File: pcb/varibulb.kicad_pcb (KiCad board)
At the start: 2 copper layers, 53.8 x 53.8 mm, 41 parts, among them IC1 ATTINY2313A-S, P1 MAINS LIVE, P2 BOARD, P3 BOARD, P5 MAINS GROUND, P6 ISP, P7 COMM, SW1 ENCODER, U1 TRIAC, U2 LM2931AZ-3.3/5.0, X1 10MHz

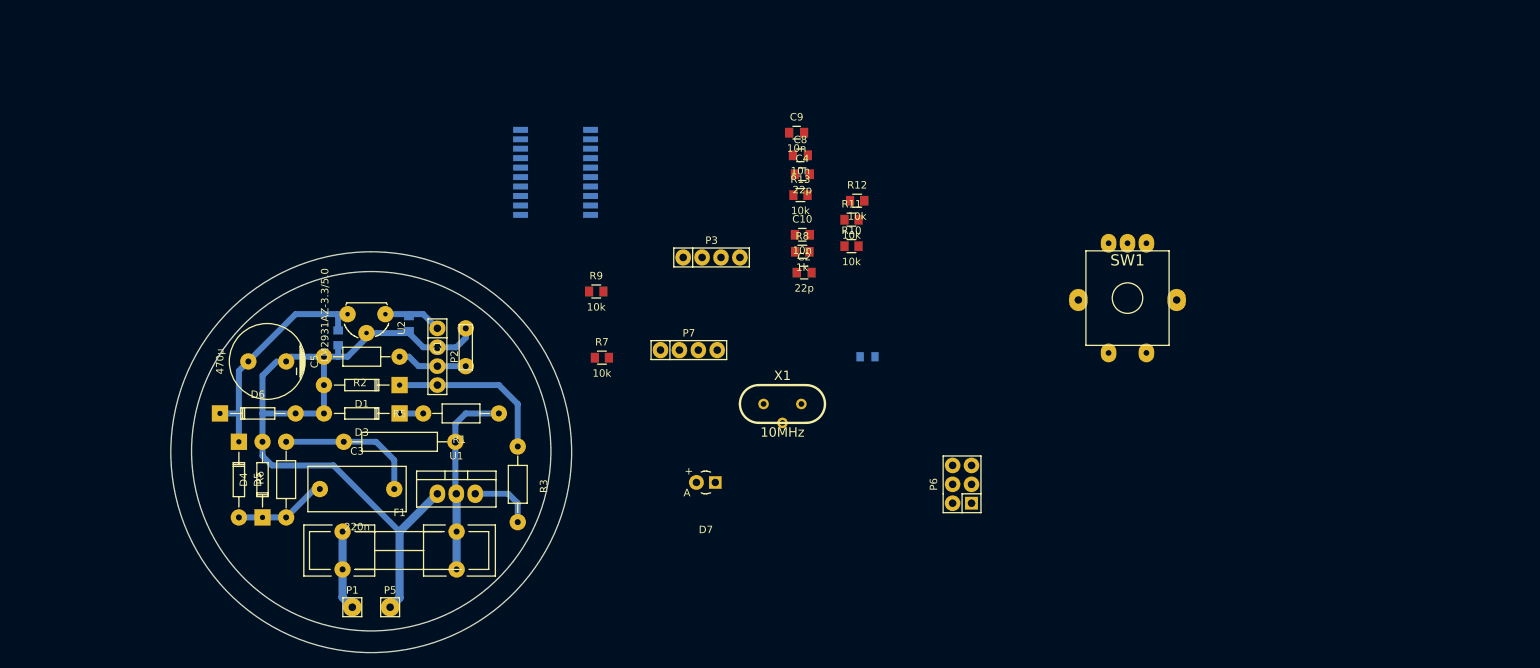
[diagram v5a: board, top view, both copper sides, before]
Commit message: move capacitor
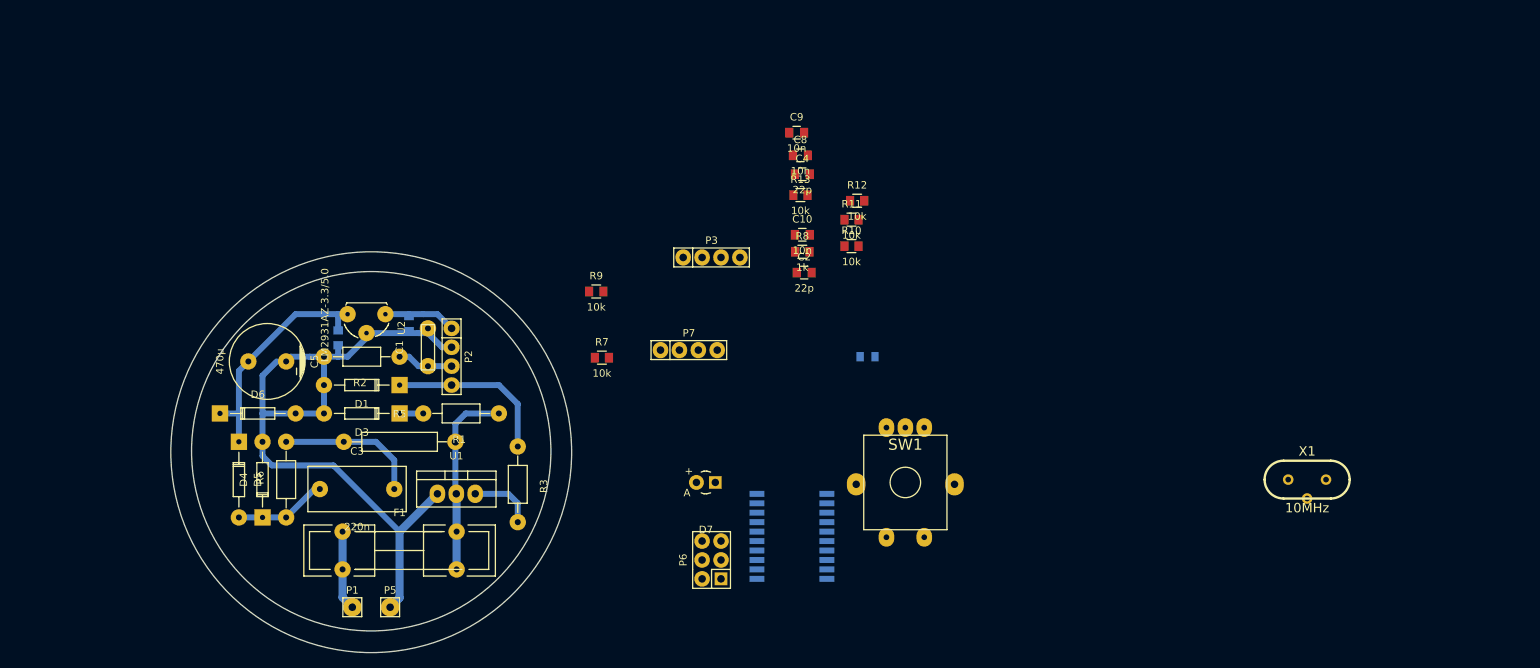
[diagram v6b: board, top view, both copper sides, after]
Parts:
- moved X1 71.2 mm to (196.8, 125.1)
- moved IC1 58.3 mm to (127.6, 132.7)
- moved SW1 38.8 mm to (142.9, 125.7)
- moved P6 35.2 mm to (116.8, 135.9)
- moved C1 5.08 mm to (78.7, 107.3)
- moved P2 1.91 mm to (81.9, 108.6)
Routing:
- net GNDREF: track 99.7 -> 97.5 mm
- net Net-(C7-Pad2): track 8.04 -> 9.95 mm
- net Net-(C1-Pad1): track 13.2 -> 11.3 mm
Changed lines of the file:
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@@
   (general
     (links 86)
-    (no_connects 52)
+    (no_connects 53)
     (area 44.755999 93.777999 98.754001 147.776001)
     (thickness 1.6)
     (drawings 2)
-    (tracks 72)
+    (tracks 73)
     (zones 0)
     (modules 41)
@@
   )
   (module Capacitors_ThroughHole:Capacitor6MMDiscRM5 (layer F.Cu)
-    (at 83.82 107.315 90)
+    (at 78.74 107.315 90)
     (descr "Capacitor 6MM Disc RM 5MM")
     (tags C)
@@
   )
   (module Pin_Headers:Pin_Header_Straight_2x03 (layer F.Cu)
-    (at 150.495 125.73 90)
+    (at 116.84 135.89 90)
     (descr "Through hole pin header")
     (tags "pin header")
@@
   )
   (module encoder:ENCODER (layer F.Cu)
-    (at 172.72 100.965 180)
+    (at 142.875 125.73 180)
     (fp_text reference SW1 (at 0 5.334 180) (layer F.SilkS)
       (effects (font (size 1.5 1.5) (thickness 0.15)))
@@
   )
   (module HC-49V:HC-49V (layer F.Cu)
-    (at 126.365 114.935)
+    (at 196.85 125.095)
     (descr "Quartz boitier HC-49 Vertical Shielded")
     (tags "QUARTZ DEV")
@@
   )
   (module Housings_SOIC:SOIC-20_7.5x12.8mm_Pitch1.27mm (layer B.Cu)
-    (at 95.885 83.82 180)
+    (at 127.635 132.715 180)
     (descr "20-Lead Plastic Small Outline (SO) - Wide, 7.50 mm Body [SOIC] (see Microchip Packaging Specification 00000049BS.pdf)")
     (tags "SOIC 1.27")
@@
   )
   (module Pin_Headers:Pin_Header_Straight_1x04 (layer F.Cu)
-    (at 80.01 108.585 270)
+    (at 81.915 108.585 270)
     (descr "Through hole pin header")
     (tags "pin header")
@@
   (segment (start 90.805 128.27) (end 89.535 127) (width 0.8) (layer B.Cu) (net 23))
   (segment (start 89.535 127) (end 85.09 127) (width 0.8) (layer B.Cu) (net 23))
-  (segment (start 80.01 109.855) (end 83.82 109.855) (width 0.8) (layer B.Cu) (net 24))
   (segment (start 74.93 108.585) (end 76.2 108.585) (width 0.8) (layer B.Cu) (net 24))
-  (segment (start 77.47 109.855) (end 80.01 109.855) (width 0.8) (layer B.Cu) (net 24))
+  (segment (start 77.47 109.855) (end 81.915 109.855) (width 0.8) (layer B.Cu) (net 24) (status 20))
   (segment (start 76.2 108.585) (end 77.47 109.855) (width 0.8) (layer B.Cu) (net 24))
   (segment (start 78.105 116.205) (end 74.93 116.205) (width 0.8) (layer B.Cu) (net 24))
   (segment (start 75.565 108.585) (end 74.93 108.585) (width 0.8) (layer B.Cu) (net 24))
-  (segment (start 56.515 120.015) (end 56.515 121.92) (width 0.8) (layer B.Cu) (net 25) (status 400000))
+  (segment (start 76.2 105.14) (end 76.2 105.41) (width 0.8) (layer B.Cu) (net 25) (status 10))
+  (segment (start 78.74 104.775) (end 78.105 105.41) (width 0.8) (layer B.Cu) (net 25))
+  (segment (start 78.105 105.41) (end 77.47 105.41) (width 0.8) (layer B.Cu) (net 25))
+  (segment (start 70.485 105.41) (end 76.2 105.41) (width 0.8) (layer B.Cu) (net 25))
+  (segment (start 76.2 105.41) (end 77.47 105.41) (width 0.8) (layer B.Cu) (net 25))
+  (segment (start 77.47 105.41) (end 78.74 105.41) (width 0.8) (layer B.Cu) (net 25))
+  (segment (start 80.645 107.315) (end 81.915 107.315) (width 0.8) (layer B.Cu) (net 25) (status 20))
+  (segment (start 78.74 105.41) (end 80.645 107.315) (width 0.8) (layer B.Cu) (net 25))
+  (segment (start 56.515 120.015) (end 56.515 121.92) (width 0.8) (layer B.Cu) (net 25))
   (segment (start 66.04 123.19) (end 57.785 123.19) (width 0.8) (layer B.Cu) (net 25))
   (segment (start 66.04 123.19) (end 74.93 132.08) (width 0.8) (layer B.Cu) (net 25))
   (segment (start 56.515 121.92) (end 57.785 123.19) (width 0.8) (layer B.Cu) (net 25))
-  (segment (start 80.01 127) (end 74.93 132.08) (width 1.1) (layer B.Cu) (net 25) (status 400000))
-  (segment (start 74.93 140.97) (end 73.66 142.24) (width 1.1) (layer B.Cu) (net 25) (status 800000))
+  (segment (start 80.01 127) (end 74.93 132.08) (width 1.1) (layer B.Cu) (net 25))
+  (segment (start 74.93 140.97) (end 73.66 142.24) (width 1.1) (layer B.Cu) (net 25))
   (segment (start 74.93 132.08) (end 74.93 140.97) (width 1.1) (layer B.Cu) (net 25))
   (segment (start 66.675 107.045) (end 66.675 108.585) (width 0.8) (layer B.Cu) (net 25))
-  (segment (start 76.2 105.14) (end 76.2 105.41) (width 0.8) (layer B.Cu) (net 25) (status 10))
-  (segment (start 70.485 105.41) (end 76.2 105.41) (width 0.8) (layer B.Cu) (net 25))
-  (segment (start 78.105 107.315) (end 80.01 107.315) (width 0.8) (layer B.Cu) (net 25))
-  (segment (start 76.2 105.41) (end 78.105 107.315) (width 0.8) (layer B.Cu) (net 25))
-  (segment (start 80.01 107.315) (end 82.55 107.315) (width 0.8) (layer B.Cu) (net 25))
-  (segment (start 83.82 106.045) (end 83.82 104.775) (width 0.8) (layer B.Cu) (net 25))
-  (segment (start 82.55 107.315) (end 83.82 106.045) (width 0.8) (layer B.Cu) (net 25))
   (segment (start 64.77 108.585) (end 66.675 108.585) (width 0.8) (layer B.Cu) (net 25))
   (segment (start 66.675 108.585) (end 67.945 108.585) (width 0.8) (layer B.Cu) (net 25))
@@
   (segment (start 90.805 114.935) (end 90.805 120.65) (width 0.8) (layer B.Cu) (net 26))
   (segment (start 88.265 112.395) (end 90.805 114.935) (width 0.8) (layer B.Cu) (net 26))
+  (segment (start 78.105 102.87) (end 80.01 102.87) (width 0.8) (layer B.Cu) (net 28))
+  (segment (start 76.2 102.87) (end 78.105 102.87) (width 0.8) (layer B.Cu) (net 28) (status 10))
+  (segment (start 80.01 102.87) (end 81.915 104.775) (width 0.8) (layer B.Cu) (net 28))
   (segment (start 76.2 103.14) (end 76.2 102.87) (width 0.8) (layer B.Cu) (net 28) (status 30))
   (segment (start 73.025 102.87) (end 76.2 102.87) (width 0.8) (layer B.Cu) (net 28) (status 20))
-  (segment (start 76.2 102.87) (end 78.105 102.87) (width 0.8) (layer B.Cu) (net 28) (status 10))
-  (segment (start 78.105 102.87) (end 80.01 104.775) (width 0.8) (layer B.Cu) (net 28))
 )

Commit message: this sucks so much..
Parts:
- R11, R12, R8: moved to B.Cu
- moved P6 96.6 mm to (195.9, 80.3), turned to 180 degrees
- moved IC1 77.5 mm to (177.8, 73.7), turned to 90 degrees
- moved P3 75.3 mm to (189.9, 76.8), turned to 270 degrees
- moved P7 74.7 mm to (188.0, 98.7)
- moved D7 67.8 mm to (179.1, 100.3)
- moved X1 58.0 mm to (165.7, 76.2), turned to 270 degrees
- moved R11 54.6 mm to (190.2, 87.0), turned to 180 degrees
- moved SW1 51.2 mm to (179.1, 89.5), turned to 270 degrees
- moved R8 46.9 mm to (175.9, 92.7), turned to 270 degrees
- moved R12 46.7 mm to (178.1, 66.7), turned to 180 degrees
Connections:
- IC1 pad 8: Net-(C8-Pad1) -> Net-(C9-Pad1)
- IC1 pad 9: Net-(C9-Pad1) -> Net-(C8-Pad1)
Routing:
- net Net-(IC1-Pad2): track 0.00 -> 38.1 mm
- net Net-(C10-Pad1): track 0.00 -> 29.5 mm
- net Net-(IC1-Pad3): track 0.00 -> 23.8 mm
- net /SENSE: track 0.00 -> 22.5 mm
- net /PHASE: track 0.00 -> 18.0 mm
- net Net-(C2-Pad1): track 0.00 -> 17.7 mm
- net Net-(C9-Pad1): track 0.00 -> 15.8 mm
- net Net-(C4-Pad1): track 0.00 -> 15.3 mm
- net Net-(IC1-Pad7): track 0.00 -> 13.4 mm
- net Net-(IC1-Pad17): track 0.00 -> 9.93 mm
- net Net-(C8-Pad1): track 0.00 -> 9.42 mm
- net Net-(IC1-Pad18): track 0.00 -> 8.27 mm
- net Net-(D7-Pad1): track 0.00 -> 7.46 mm
- net VCC: track 0.00 -> 6.36 mm
- net Net-(IC1-Pad19): track 0.00 -> 6.10 mm
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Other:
- board size 53.8 x 53.8 mm -> 161.8 x 85.6 mm

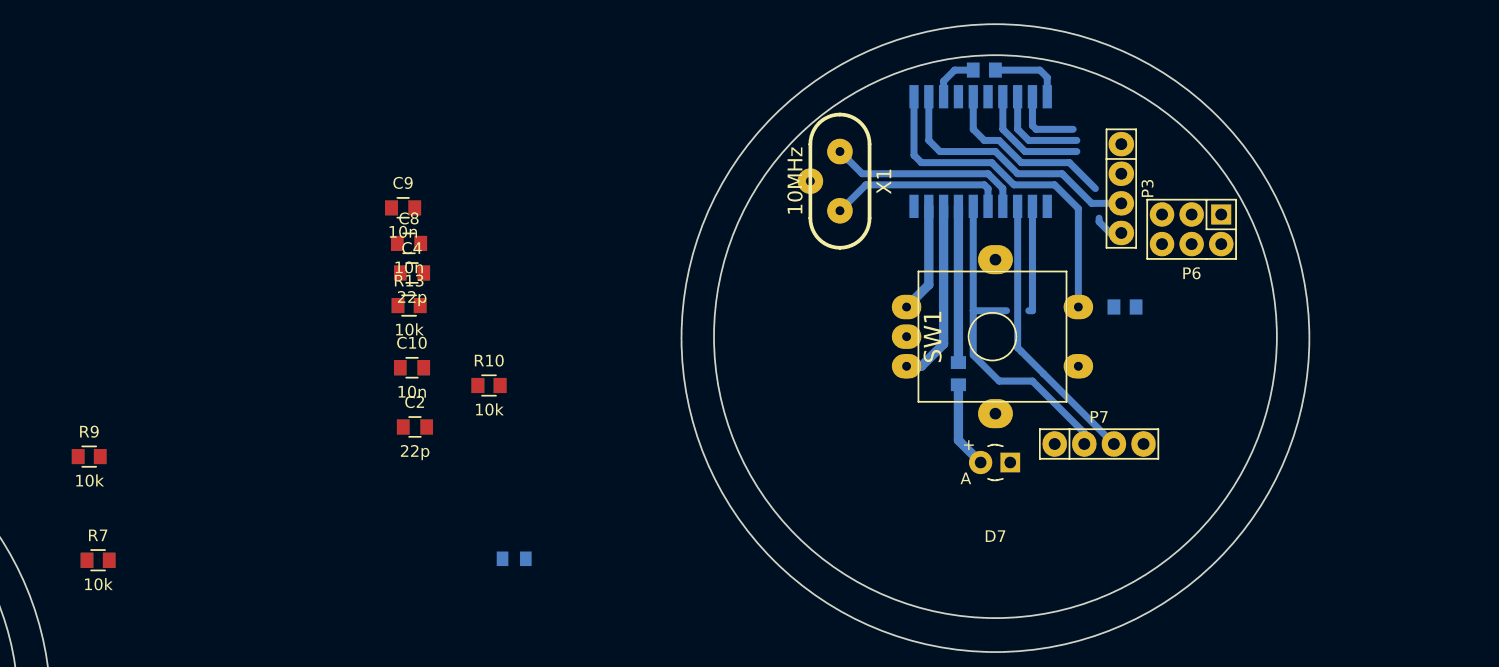
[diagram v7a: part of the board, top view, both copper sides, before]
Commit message: arrange some more components
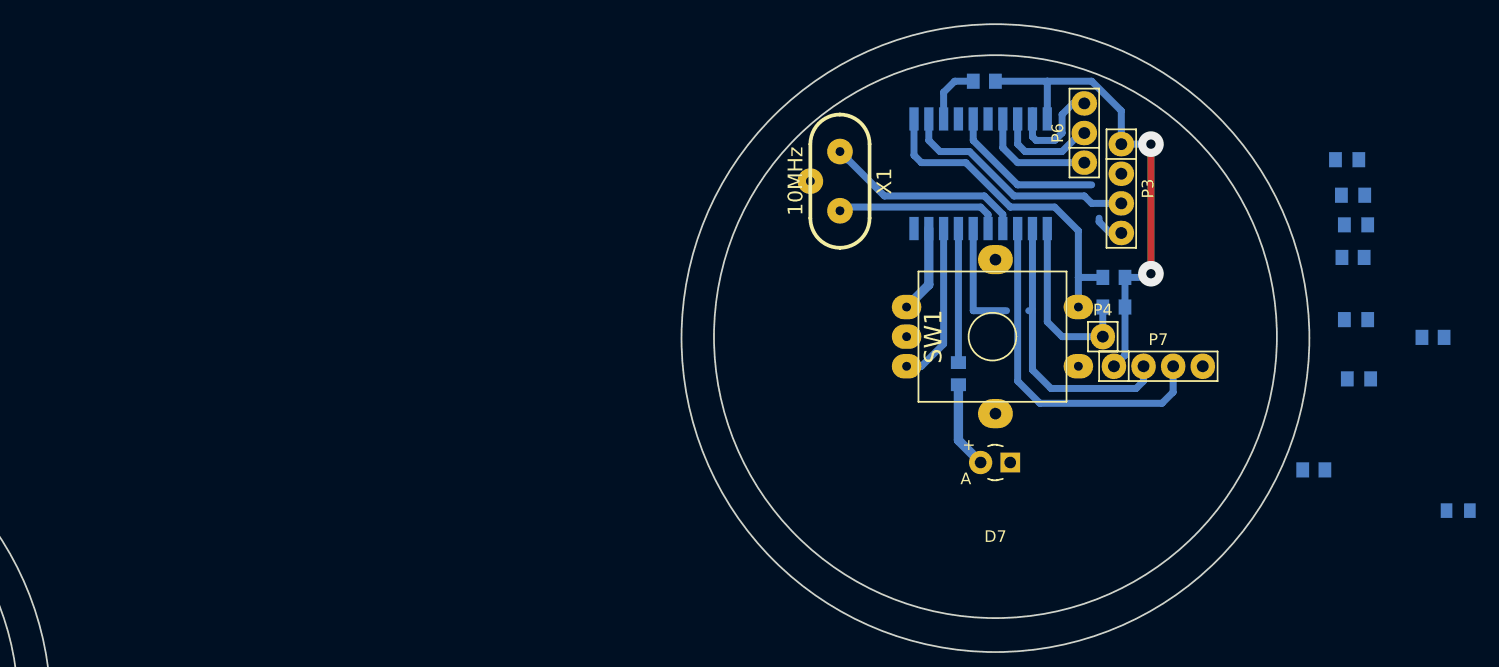
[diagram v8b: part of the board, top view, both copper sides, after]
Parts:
- added P4: RESET, Pin_Headers:Pin_Header_Straight_1x01, F.Cu at (188.3, 89.5)
- C10, C2, C4, C8, C9, R10, R13, R7, R9: moved to B.Cu
- P6: footprint Pin_Headers:Pin_Header_Straight_2x03 -> Pin_Headers:Pin_Header_Straight_1x03
- moved R9 105.0 mm to (206.4, 101.0)
- moved R7 89.8 mm to (189.2, 87.0)
- moved C11 81.1 mm to (218.8, 104.5)
- moved C2 81.1 mm to (210.2, 93.2)
- moved C8 81.1 mm to (209.7, 77.4)
- moved R10 81.1 mm to (216.6, 89.6)
- moved R13 81.1 mm to (209.7, 82.7)
- moved C10 81.1 mm to (210.0, 88.1)
- moved C4 81.1 mm to (210.0, 79.9)
- moved C9 81.1 mm to (209.2, 74.4)
- moved P6 12.4 mm to (186.7, 72.1), turned to 90 degrees
- moved P7 8.38 mm to (193.0, 92.1)
- moved R11 2.71 mm to (189.2, 84.5)
- moved IC1 1.91 mm to (177.8, 75.6)
- moved R12 0.95 mm to (178.1, 67.6)
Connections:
- P6 pad 1: Net-(IC1-Pad18) -> Net-(IC1-Pad17)
- P6 pad 2: VCC -> Net-(IC1-Pad18)
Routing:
- net VCC: track 6.36 -> 42.0 mm, vias 0 -> 2
- net Net-(IC1-Pad1): track 0.00 -> 15.8 mm
- net Net-(IC1-Pad3): track 23.8 -> 29.8 mm
- net Net-(IC1-Pad2): track 38.1 -> 34.1 mm
- net Net-(IC1-Pad19): track 6.10 -> 9.04 mm
- net Net-(IC1-Pad7): track 13.4 -> 11.5 mm
- net Net-(C9-Pad1): track 15.8 -> 13.9 mm
- net Net-(C8-Pad1): track 9.42 -> 7.52 mm
- net /SENSE: track 22.5 -> 20.6 mm
- net /PHASE: track 18.0 -> 16.2 mm
- net Net-(C4-Pad1): track 15.3 -> 14.3 mm
- net Net-(IC1-Pad13): track 4.27 -> 5.22 mm
- net Net-(IC1-Pad18): track 8.27 -> 9.05 mm
- net Net-(C2-Pad1): track 17.7 -> 18.3 mm
- net Net-(C10-Pad1): track 29.5 -> 28.9 mm
